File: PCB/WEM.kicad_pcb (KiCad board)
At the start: 2 copper layers, 8.6 x 17.3 mm, 77 parts, among them J1 USB_C_Receptacle_USB2.0_14P, J2 MCU flashing pins, J3 Extensions' connectors, J4 Battery, J5 Reset, SW1 Kailh Mouse Scroll Wheel Enco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, SW2 LMB, SW3 MMB, SW4 RMB, SW5 FORWARD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

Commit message: Schematics modifications and firmware
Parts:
- removed SW9: Power/mode switch, SW-TH_SSSS223600:SW-TH_SSSS223600
- added C32: 10nF, Capacitor_SMD:C_0805_2012Metric_Pad1.18x1.45mm_HandSolder, F.Cu at (129.0, 71.1)
- added J6: Battery jumper, Connector_PinHeader_2.54mm:PinHeader_1x02_P2.54mm_Vertical, F.Cu at (109.2, 101.6)
- added R11: 4M, Resistor_SMD:R_0805_2012Metric_Pad1.20x1.40mm_HandSolder, F.Cu at (128.8, 86.1)
- added R12: 10M, Resistor_SMD:R_0805_2012Metric_Pad1.20x1.40mm_HandSolder, F.Cu at (128.8, 89.0)
- added SW8: ON/OFF, Kailh:Kailh MI627301D07, F.Cu at (107.9, 78.8)
- D6: footprint Diode_THT:D_DO-41_SOD81_P10.16mm_Horizontal -> Diode_SMD:D_SOD-323F
- moved SW1 123.2 mm to (225.9, 65.0), turned to 90 degrees
- moved AE1 110.4 mm to (196.6, 69.8), turned to 63 degrees
- moved J1 108.2 mm to (218.0, 56.0), turned to 180 degrees
- moved SW4 107.1 mm to (224.0, 55.0)
- moved SW2 97.7 mm to (206.0, 55.0)
- moved SW3 97.5 mm to (206.0, 65.0)
- moved U1 57.8 mm to (136.4, 69.6)
- moved SW5 56.8 mm to (157.0, 41.0)
- moved D3 54.7 mm to (146.9, 76.2)
- moved D4 54.7 mm to (146.9, 79.2)
- moved D5 54.7 mm to (146.9, 82.3)
- moved U2 49.5 mm to (98.7, 106.9)
- moved D6 46.6 mm to (133.0, 105.9)
- moved J3 39.5 mm to (100.0, 93.8)
- moved SW6 33.9 mm to (137.0, 42.0)
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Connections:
- AE1 pad 2: (no net) -> GND
- U1 pad A12: unconnected-(U1-AIN0/P0.02-PadA12) -> Net-(U1-AIN0/P0.02)
- U1 pad AD20: unconnected-(U1-P0.24-PadAD20) -> OPTSENSE_RESET
- U1 pad P2: BLE_MODE -> unconnected-(U1-P1.08-PadP2)
- U1 pad P23: DONGLE_MODE -> POWER_SWITCH
- U3 pad 14: Net-(U3-NRESET) -> OPTSENSE_RESET
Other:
- board size 8.6 x 17.3 mm -> 50 x 60 mm

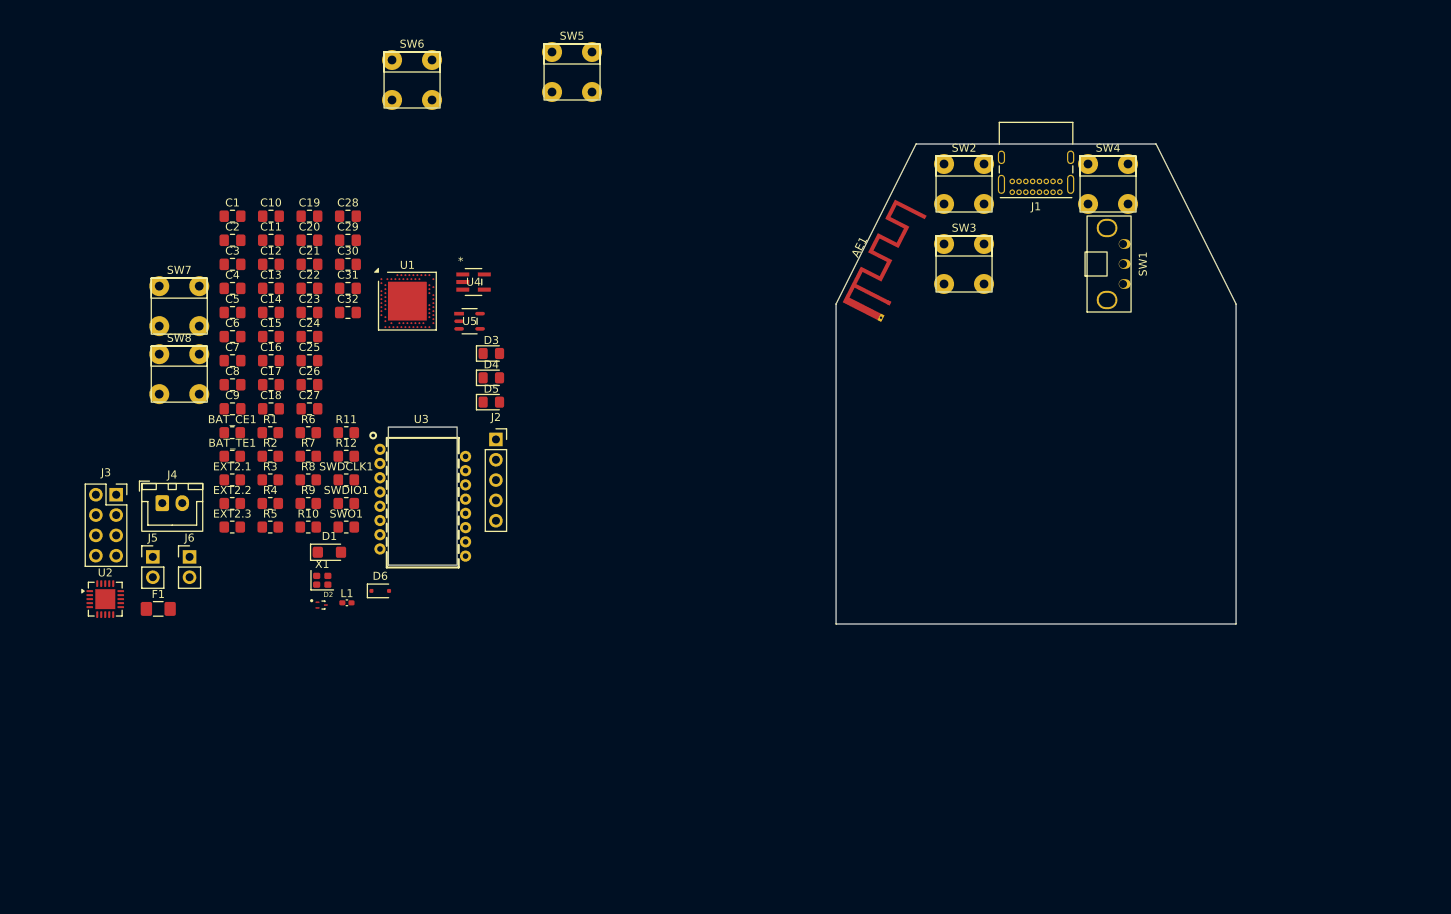
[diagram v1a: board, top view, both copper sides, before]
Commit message: Started PCB routing
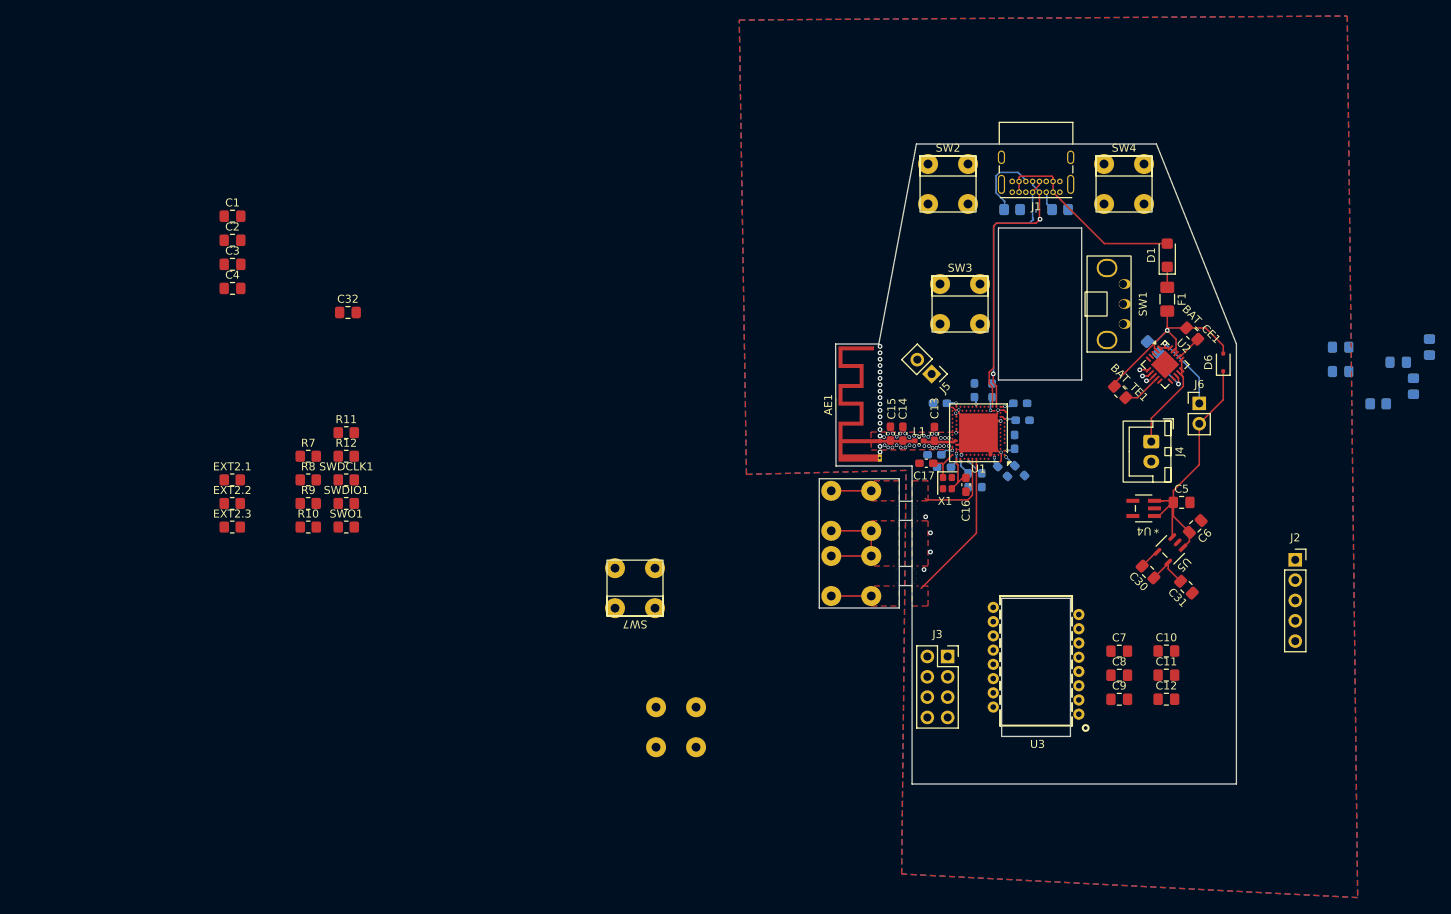
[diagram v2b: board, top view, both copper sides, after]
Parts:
- C13, C14, C15, C16, C17: footprint Capacitor_SMD:C_0805_2012Metric_Pad1.18x1.45mm_HandSolder -> Capacitor_SMD:C_0603_1608Metric_Pad1.08x0.95mm_HandSolder
- C18, C19, C20, C21, C22, C23, C24, C25, C26, C27, C28, C29: footprint Capacitor_SMD:C_0805_2012Metric_Pad1.18x1.45mm_HandSolder -> Capacitor_SMD:C_0603_1608Metric_Pad1.08x0.95mm_HandSolder; moved to B.Cu
- D2, D3, D4, D5, R1, R2, R3, R4, R5, R6, SW5, SW6, SW8: moved to B.Cu
- moved R4 146.2 mm to (264.2, 75.4), turned to -90 degrees
- moved R5 144.0 mm to (262.2, 80.3), turned to -90 degrees
- moved R3 138.8 mm to (257.8, 82.5), turned to 180 degrees
- moved U2 135.7 mm to (231.1, 77.6), turned to -45 degrees
- moved F1 131.9 mm to (231.4, 69.4), turned to -90 degrees
- moved J6 127.7 mm to (235.4, 82.4)
- moved C10 124.4 mm to (231.3, 113.4)
- moved C11 124.4 mm to (231.3, 116.4)
- moved C12 124.4 mm to (231.3, 119.4)
- moved J4 123.9 mm to (229.4, 87.2), turned to -90 degrees
- moved C6 122.7 mm to (234.9, 97.8), turned to 45 degrees
- moved C5 121.0 mm to (233.2, 94.8)
- moved BAT_CE1 120.6 mm to (234.5, 73.7), turned to -45 degrees
- moved C7 116.6 mm to (225.4, 113.4)
- moved C8 116.6 mm to (225.4, 116.4)
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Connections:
- U1 pad A14: unconnected-(U1-P1.15-PadA14) -> BACK
- U1 pad A16: unconnected-(U1-P1.13-PadA16) -> FORWARD
- U1 pad A8: unconnected-(U1-AIN7/P0.31-PadA8) -> OPTSENSE_SCLK
- U1 pad AC11: MMB -> unconnected-(U1-P0.16-PadAC11)
- U1 pad AC15: OPTSENSE_CS -> unconnected-(U1-P0.19-PadAC15)
- U1 pad AC17: OPTSENSE_MISO -> unconnected-(U1-P0.21-PadAC17)
- U1 pad AC19: OPTSENSE_SCLK -> unconnected-(U1-P0.23-PadAC19)
- U1 pad AC9: BACK -> unconnected-(U1-P0.14-PadAC9)
- U1 pad AD8: FORWARD -> EXT2.1
- U1 pad B11: EXT2.1 -> unconnected-(U1-AIN4/P0.28-PadB11)
- U1 pad B9: EXT2.3 -> unconnected-(U1-AIN6/P0.30-PadB9)
- U1 pad F2: unconnected-(U1-XL2/P0.01-PadF2) -> RE_B
- U1 pad H2: RE_B -> unconnected-(U1-P0.27-PadH2)
- U1 pad J1: unconnected-(U1-AIN2/P0.04-PadJ1) -> MMB
- U1 pad J24: unconnected-(U1-NFC2/P0.10-PadJ24) -> EXT1.5
- U1 pad L1: unconnected-(U1-P0.06-PadL1) -> EXT2.3
- U1 pad L24: unconnected-(U1-NFC1/P0.09-PadL24) -> EXT1.3
- U1 pad N1: unconnected-(U1-P0.08-PadN1) -> OPTSENSE_CS
- U1 pad R1: unconnected-(U1-TRACEDATA3/P1.09-PadR1) -> OPTSENSE_MISO
- U1 pad T23: EXT1.5 -> unconnected-(U1-P1.05-PadT23)
- U1 pad V23: EXT1.3 -> unconnected-(U1-P1.03-PadV23)
- X1 pad 1: Net-(U1-XC2) -> Net-(U1-XC1)
- X1 pad 2: Net-(U1-XC1) -> GND
- X1 pad 3: (no net) -> Net-(U1-XC2)
- X1 pad 4: (no net) -> GND
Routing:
- net POWER: track 0.00 -> 39.1 mm
- net GND: track 0.00 -> 38.9 mm, vias 0 -> 58
- net USB_D+: track 0.00 -> 34.3 mm, vias 0 -> 1
- net USB_D-: track 0.00 -> 33.2 mm, vias 0 -> 1
- net VBUS: track 0.00 -> 30.9 mm, vias 0 -> 2
- net Net-(D1-A2): track 0.00 -> 25.1 mm
- net BACK: track 0.00 -> 24.1 mm
- net FORWARD: track 0.00 -> 15.8 mm
- net +BATT: track 0.00 -> 12.8 mm
- net BATOUT: track 0.00 -> 11.3 mm, vias 0 -> 1
- net +3V3: track 0.00 -> 10.1 mm, vias 0 -> 5
- net Net-(J1-CC2): track 0.00 -> 9.15 mm
- net Net-(U2-PROG1): track 0.00 -> 6.15 mm, vias 0 -> 1
- net +2V: track 0.00 -> 5.63 mm
- net Net-(U1-XC2): track 0.00 -> 5.37 mm
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- added copper zone on F.Cu, net BACK
- added copper zone on F.Cu, net FORWARD
- added copper zone on B.Cu, net GND
- added copper zone on F.Cu, net GND
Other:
- board size 50 x 60 mm -> 52.1 x 80 mm

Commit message: Continued routing. It's hopeless
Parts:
- removed J5: Reset, Connector_PinHeader_2.54mm:PinHeader_1x02_P2.54mm_Vertical
- removed R10, R9: 10K, Resistor_SMD:R_0805_2012Metric_Pad1.20x1.40mm_HandSolder
- C1, C10, C11, C12, C2, C3, C32, C4, C7, C8, C9, EXT2.1, EXT2.2, EXT2.3, R11, R12, R7, R8, SWDCLK1, SWDIO1, SWO1: moved to B.Cu
- moved C2 122.4 mm to (235.8, 78.1), turned to 45 degrees
- moved C1 120.2 mm to (233.8, 73.8), turned to 45 degrees
- moved C3 118.2 mm to (231.2, 83.7), turned to 105 degrees
- moved EXT2.3 117.7 mm to (229.6, 122.8)
- moved C4 117.0 mm to (227.2, 100.0), turned to -90 degrees
- moved EXT2.2 113.5 mm to (224.8, 121.8), turned to 90 degrees
- moved EXT2.1 111.1 mm to (221.6, 121.8), turned to 90 degrees
- moved SWDCLK1 107.7 mm to (234.0, 115.0)
- moved SWO1 107.4 mm to (234.0, 119.2), turned to 180 degrees
- moved SWDIO1 106.4 mm to (234.0, 110.6)
- moved R7 102.1 mm to (222.4, 116.2), turned to 90 degrees
- moved R11 89.3 mm to (217.7, 94.5), turned to 180 degrees
- moved R12 85.4 mm to (213.9, 95.8), turned to -90 degrees
- moved C32 84.8 mm to (210.1, 95.8), turned to -90 degrees
- moved R8 83.8 mm to (206.8, 105.2), turned to 90 degrees
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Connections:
- U1 pad AC13: Net-(J5-Pin_1) -> unconnected-(U1-P0.18/~{RESET}-PadAC13)
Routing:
- net SWDCLK: track 0.00 -> 56.9 mm, vias 0 -> 5
- net SWO: track 0.00 -> 55.4 mm, vias 0 -> 5
- net SWDIO: track 0.00 -> 52.8 mm, vias 0 -> 5
- net EXT2.3: track 0.00 -> 46.8 mm, vias 0 -> 3
- net RMB: track 0.00 -> 46.1 mm, vias 0 -> 1
- net OPTSENSE_RESET: track 0.00 -> 43.3 mm, vias 0 -> 3
- net OPTSENSE_MOSI: track 0.00 -> 43.1 mm, vias 0 -> 2
- net MOTION: track 0.00 -> 41.0 mm, vias 0 -> 2
- net POWER_SWITCH: track 0.52 -> 38.1 mm, vias 1 -> 2
- net +3V3: track 10.1 -> 46.4 mm, vias 5 -> 6
- net OPTSENSE_MISO: track 0.00 -> 34.0 mm, vias 0 -> 2
- net OPTSENSE_CS: track 0.00 -> 32.3 mm, vias 0 -> 2
- net VBUS: track 30.9 -> 60.4 mm
- net MMB: track 0.00 -> 26.5 mm, vias 0 -> 1
- net LMB: track 0.00 -> 26.2 mm
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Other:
- board size 52.1 x 80 mm -> 52.2 x 80 mm
